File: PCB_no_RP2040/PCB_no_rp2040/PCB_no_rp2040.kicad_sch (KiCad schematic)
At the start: 7 parts, among them U1 74HC595, U2 74HC595, U3 74HC595, U4 74HC595, U5 74HC595, U6 74HC595, U7 74HC595

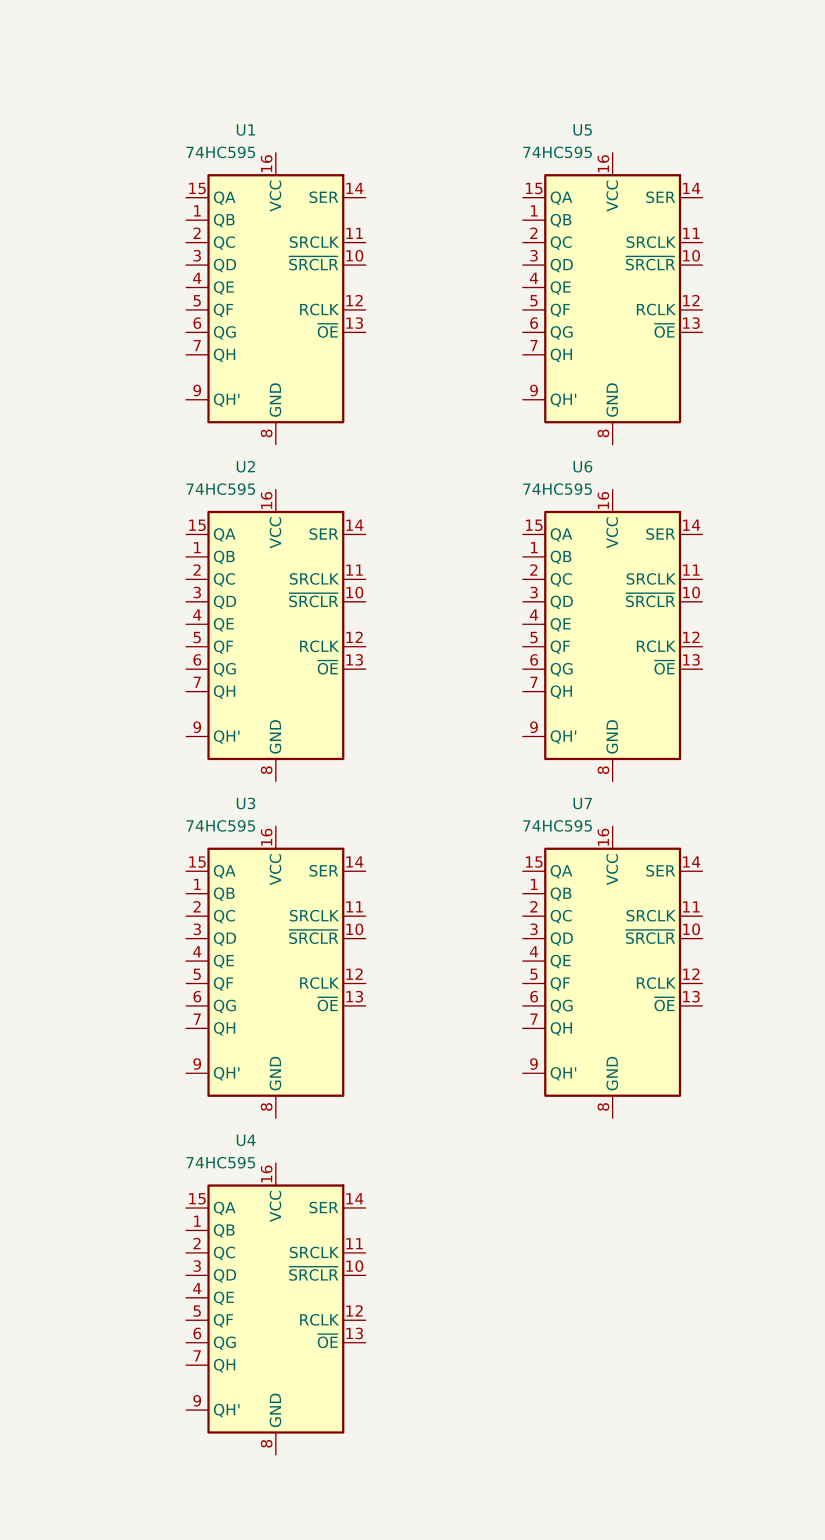
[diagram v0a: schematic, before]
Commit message: Added 4/7 shift registers and connected them to connection block, I believe this could be improved with bus lines
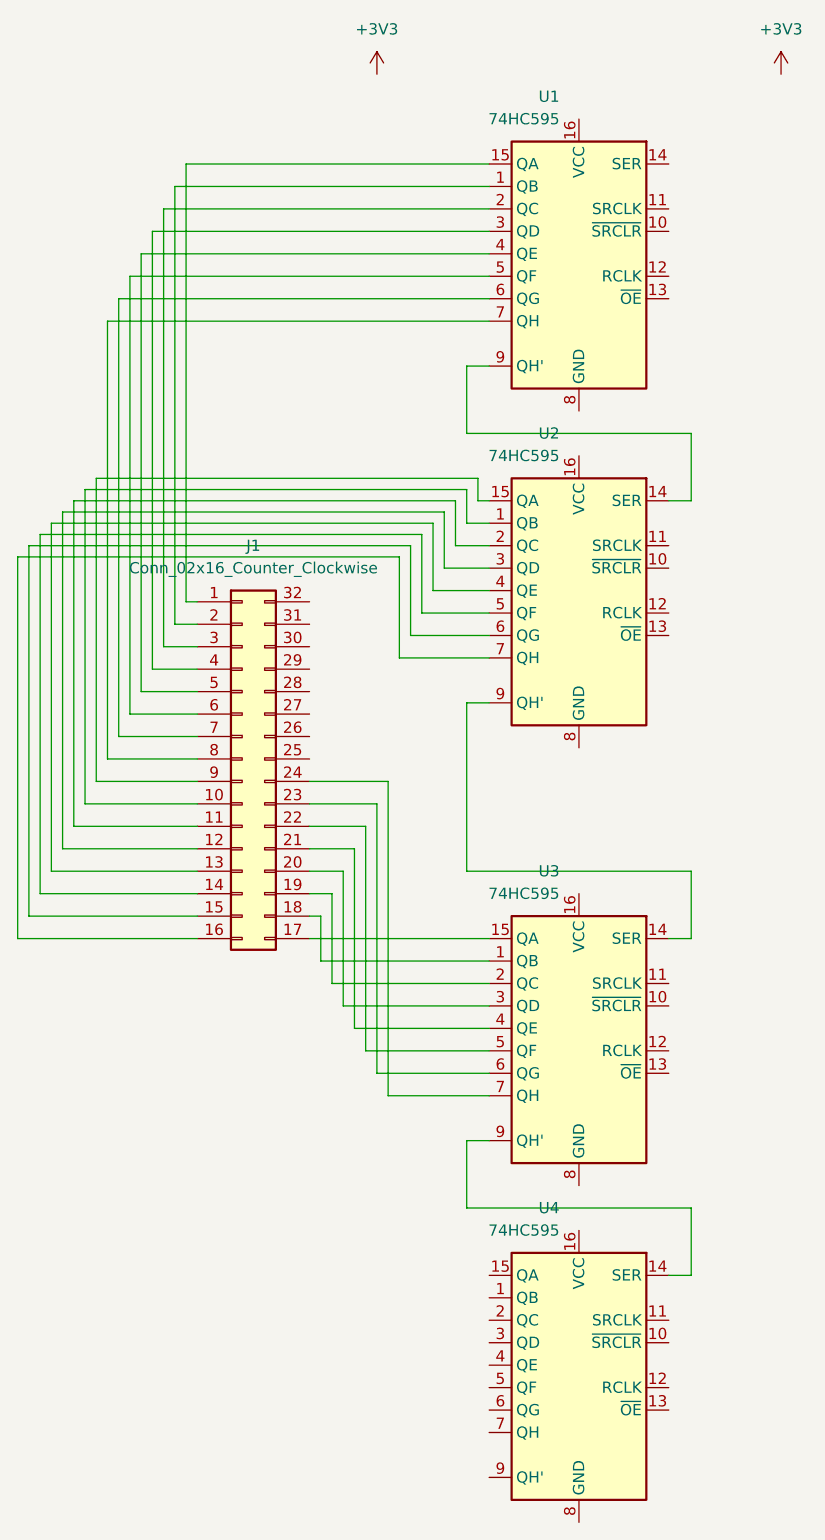
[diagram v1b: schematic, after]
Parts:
- removed U5, U6, U7: 74HC595, symbol 74xx:74HC595
- added J1: Conn_02x16_Counter_Clockwise, symbol Connector_Generic:Conn_02x16_Counter_Clockwise
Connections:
- net at U3.1 (QB): now also J1.18 (Pin_18)
- net at U3.14 (SER): now also U2.9 (QH')
- net at U3.15 (QA): now also J1.17 (Pin_17)
- net at U3.2 (QC): now also J1.19 (Pin_19)
- net at U3.3 (QD): now also J1.20 (Pin_20)
- net at U3.4 (QE): now also J1.21 (Pin_21)
- net at U3.5 (QF): now also J1.22 (Pin_22)
- net at U3.6 (QG): now also J1.23 (Pin_23)
- net at U3.7 (QH): now also J1.24 (Pin_24)
- net at U3.9 (QH'): now also U4.14 (SER)
- net at U2.1 (QB): now also J1.10 (Pin_10)
- net at U2.14 (SER): now also U1.9 (QH')
- net at U2.15 (QA): now also J1.9 (Pin_9)
- net at U2.2 (QC): now also J1.11 (Pin_11)
- net at U2.3 (QD): now also J1.12 (Pin_12)
- net at U2.4 (QE): now also J1.13 (Pin_13)
- net at U2.5 (QF): now also J1.14 (Pin_14)
- net at U2.6 (QG): now also J1.15 (Pin_15)
- net at U2.7 (QH): now also J1.16 (Pin_16)
- net at U1.1 (QB): now also J1.2 (Pin_2)
- net at U1.15 (QA): now also J1.1 (Pin_1)
- net at U1.2 (QC): now also J1.3 (Pin_3)
- net at U1.3 (QD): now also J1.4 (Pin_4)
- net at U1.4 (QE): now also J1.5 (Pin_5)
- net at U1.5 (QF): now also J1.6 (Pin_6)
- net at U1.6 (QG): now also J1.7 (Pin_7)
- net at U1.7 (QH): now also J1.8 (Pin_8)
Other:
- moved on the sheet: U1, U2, U3, U4

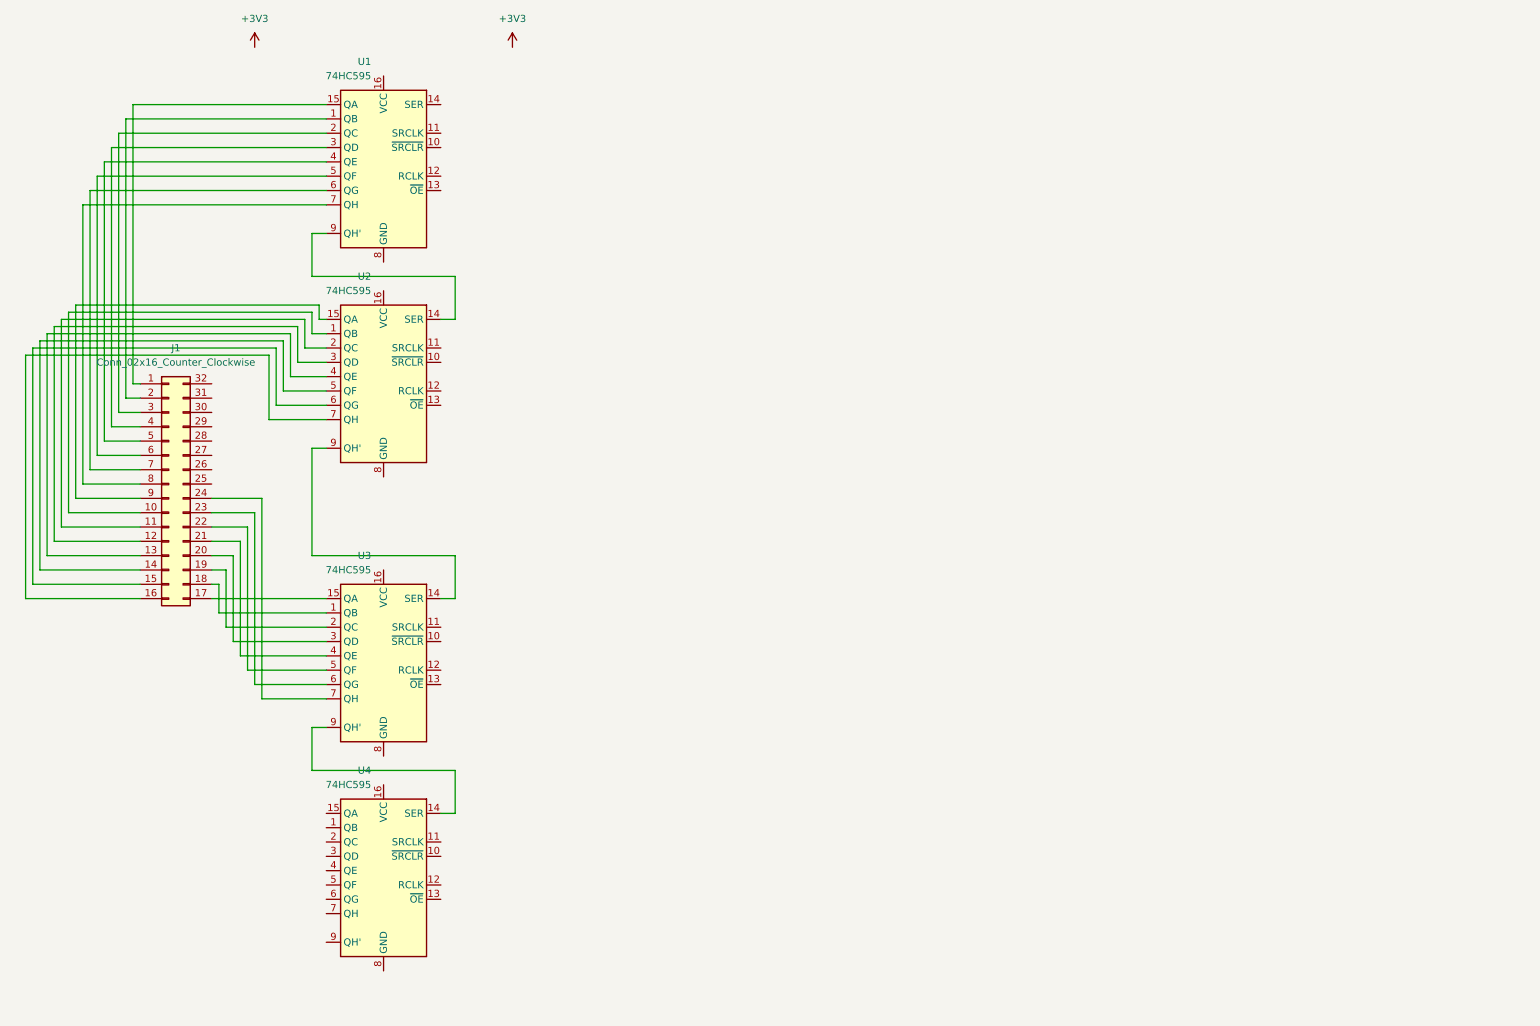
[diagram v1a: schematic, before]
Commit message: Added 7/7 shift registers with fully connected inputs and outputs, need to look into necesity of decoupling capacitor on GND
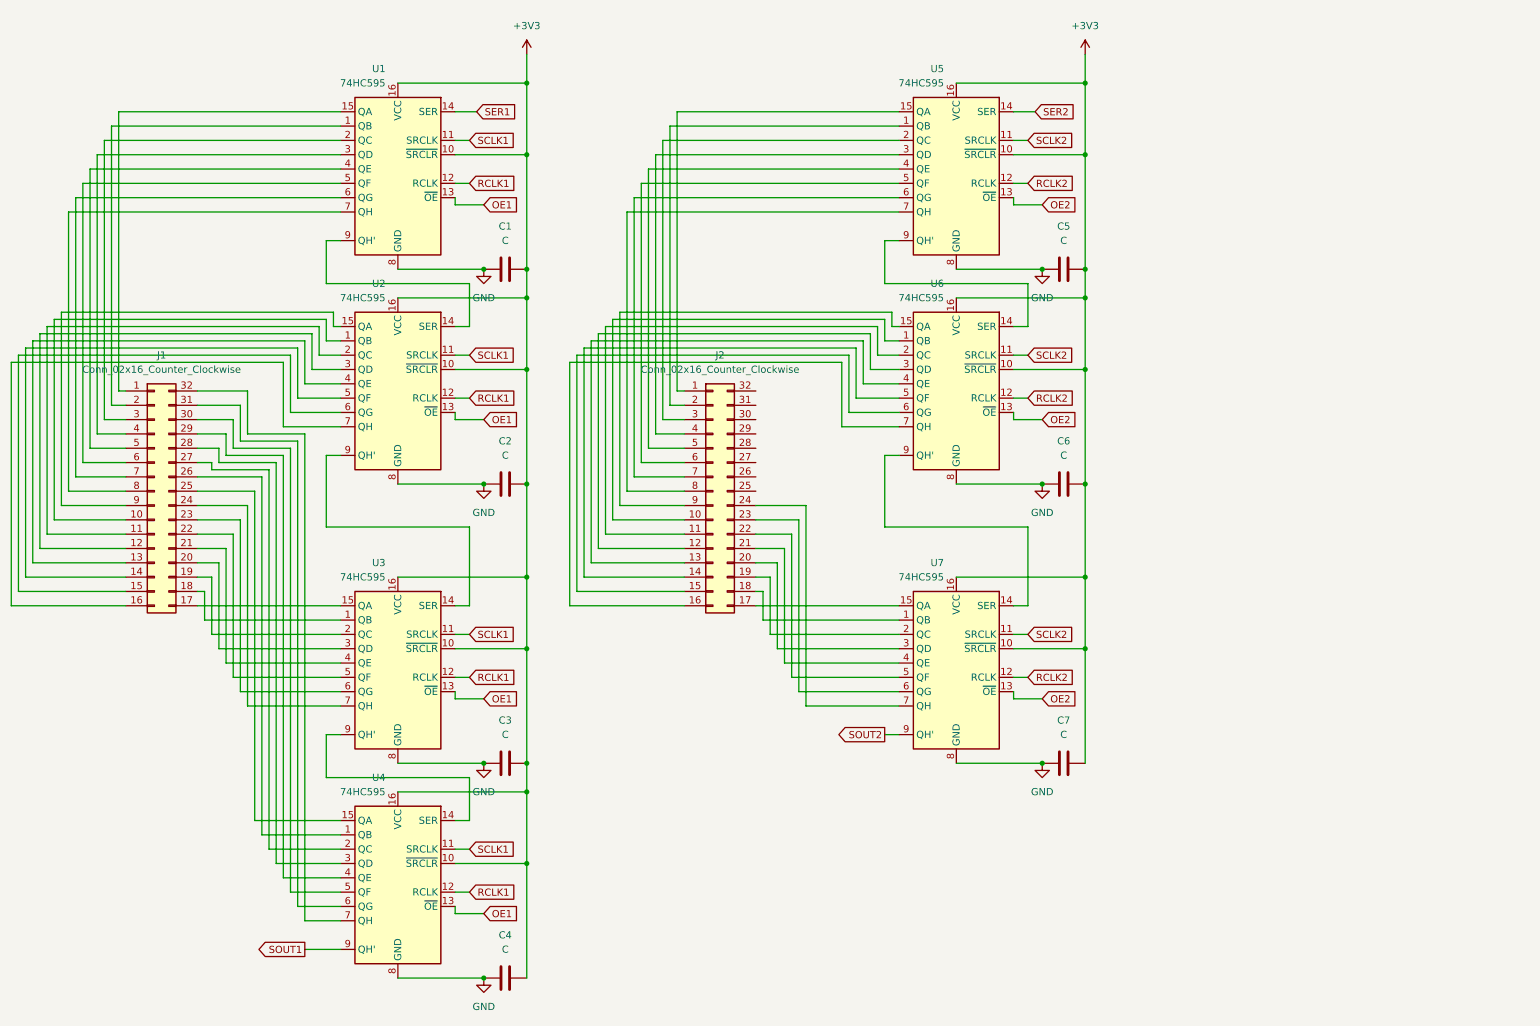
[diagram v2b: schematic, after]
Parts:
- added C1, C2, C3, C4, C5, C6, C7: C, symbol Device:C
- added J2: Conn_02x16_Counter_Clockwise, symbol Connector_Generic:Conn_02x16_Counter_Clockwise
- added U5, U6, U7: 74HC595, symbol 74xx:74HC595
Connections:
- net +3V3: now also U1.10 (~{SRCLR}), U1.16 (VCC), U2.10 (~{SRCLR}), U2.16 (VCC), U3.10 (~{SRCLR}), U3.16 (VCC), U4.10 (~{SRCLR}), U4.16 (VCC), C1.1, C2.1, C3.1, C4.1, C5.1, C6.1, C7.1, U5.10 (~{SRCLR}), U5.16 (VCC), U6.10 (~{SRCLR}), U6.16 (VCC), U7.10 (~{SRCLR}), U7.16 (VCC)
- net at J1.25 (Pin_25): now also U4.15 (QA)
- net at J1.26 (Pin_26): now also U4.1 (QB)
- net at J1.27 (Pin_27): now also U4.2 (QC)
- net at J1.28 (Pin_28): now also U4.3 (QD)
- net at J1.29 (Pin_29): now also U4.4 (QE)
- net at J1.30 (Pin_30): now also U4.5 (QF)
- net at J1.31 (Pin_31): now also U4.6 (QG)
- net at J1.32 (Pin_32): now also U4.7 (QH)
- net SCLK1: now reaches U3.11 (SRCLK)
- net SCLK1: now also U1.11 (SRCLK), U2.11 (SRCLK), U4.11 (SRCLK)
- net RCLK1: now reaches U3.12 (RCLK)
- net RCLK1: now also U1.12 (RCLK), U2.12 (RCLK), U4.12 (RCLK)
- net OE1: now reaches U3.13 (~{OE})
- net OE1: now also U1.13 (~{OE}), U2.13 (~{OE}), U4.13 (~{OE})
- net GND: now reaches U3.8 (GND)
- net GND: now also U1.8 (GND), U2.8 (GND), U4.8 (GND), C1.2, C2.2, C3.2, C4.2, C5.2, C6.2, C7.2, U5.8 (GND), U6.8 (GND), U7.8 (GND)
- net SOUT1: now reaches U4.9 (QH')
- net SER1: now reaches U1.14 (SER)
- new net: J2.2 (Pin_2), U5.1 (QB)
- new net: J2.1 (Pin_1), U5.15 (QA)
- new net: J2.3 (Pin_3), U5.2 (QC)
- new net: J2.4 (Pin_4), U5.3 (QD)
- new net: J2.5 (Pin_5), U5.4 (QE)
- new net: J2.6 (Pin_6), U5.5 (QF)
- new net: J2.7 (Pin_7), U5.6 (QG)
- new net: J2.8 (Pin_8), U5.7 (QH)
- new net: U5.9 (QH'), U6.14 (SER)
- new net: J2.18 (Pin_18), U7.1 (QB)
- new net: U6.9 (QH'), U7.14 (SER)
- new net: J2.17 (Pin_17), U7.15 (QA)
- new net: J2.19 (Pin_19), U7.2 (QC)
- new net: J2.20 (Pin_20), U7.3 (QD)
- new net: J2.21 (Pin_21), U7.4 (QE)
- new net: J2.22 (Pin_22), U7.5 (QF)
- new net: J2.23 (Pin_23), U7.6 (QG)
- new net: J2.24 (Pin_24), U7.7 (QH)
- new net: J2.10 (Pin_10), U6.1 (QB)
- new net: J2.11 (Pin_11), U6.2 (QC)
- new net: J2.12 (Pin_12), U6.3 (QD)
- new net: J2.13 (Pin_13), U6.4 (QE)
- new net: J2.14 (Pin_14), U6.5 (QF)
- new net: J2.15 (Pin_15), U6.6 (QG)
- new net: J2.16 (Pin_16), U6.7 (QH)
- new net: J2.9 (Pin_9), U6.15 (QA)
- new net OE2: U5.13 (~{OE}), U6.13 (~{OE}), U7.13 (~{OE})
- new net RCLK2: U5.12 (RCLK), U6.12 (RCLK), U7.12 (RCLK)
- new net SCLK2: U5.11 (SRCLK), U6.11 (SRCLK), U7.11 (SRCLK)
- new net SER2: U5.14 (SER)
- new net SOUT2: U7.9 (QH')
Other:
- moved on the sheet: J1, U1, U2, U3, U4

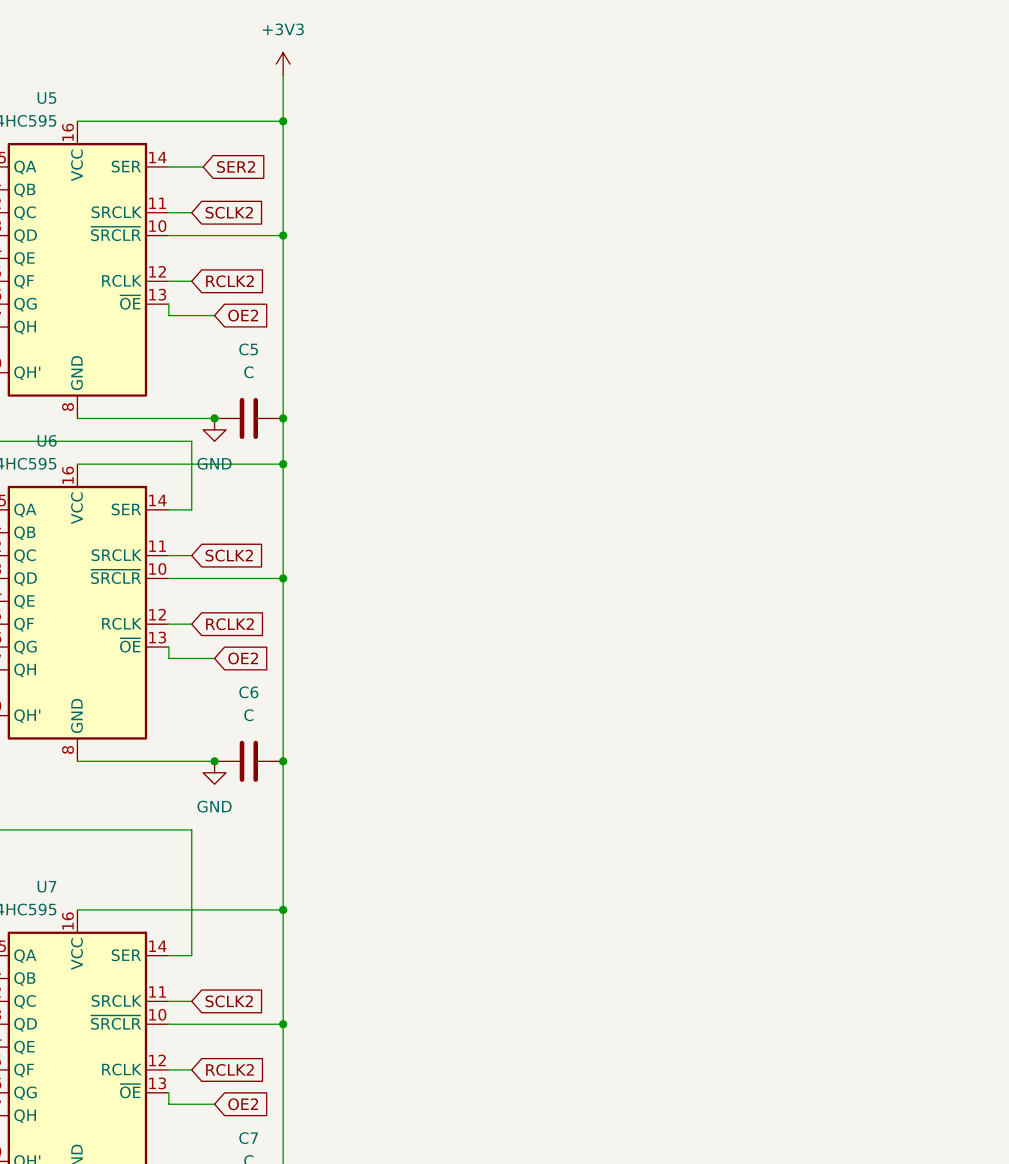
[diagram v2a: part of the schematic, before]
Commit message: Added both ADC's connected all inputs that connect to the mat, but need to look into what other pins do before connecting them
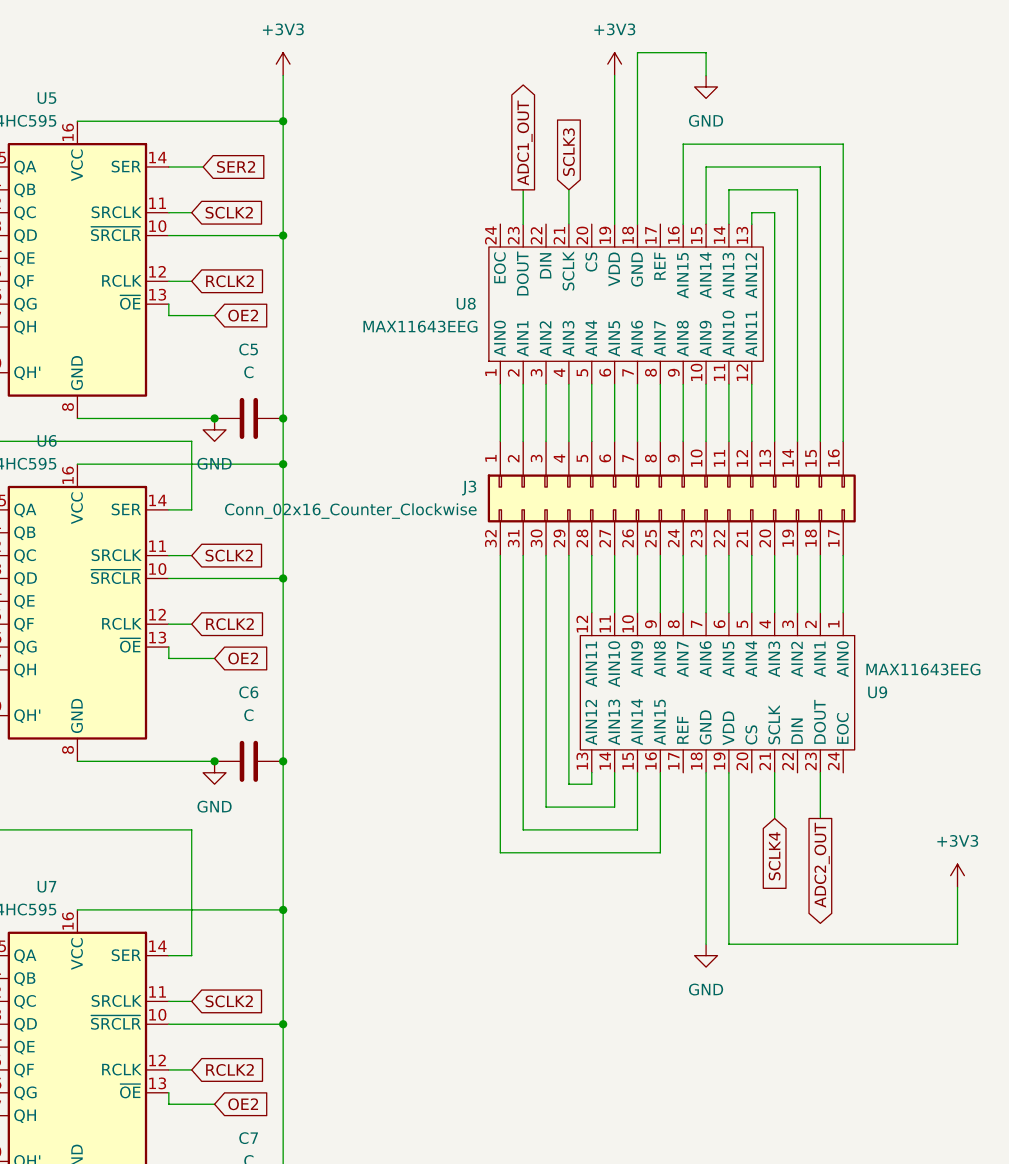
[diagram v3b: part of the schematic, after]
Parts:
- added J3: Conn_02x16_Counter_Clockwise, symbol Connector_Generic:Conn_02x16_Counter_Clockwise
- added U8, U9: MAX11643EEG, symbol Capstone_Library:MAX11643EEG
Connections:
- net +3V3: now also U8.19 (VDD), U9.19 (VDD)
- net GND: now also U8.18 (GND), U9.18 (GND)
- new net: J3.1 (Pin_1), U8.1 (AIN0)
- new net: J3.10 (Pin_10), U8.10 (AIN9)
- new net: J3.11 (Pin_11), U8.11 (AIN10)
- new net: J3.12 (Pin_12), U8.12 (AIN11)
- new net: J3.13 (Pin_13), U8.13 (AIN12)
- new net: J3.14 (Pin_14), U8.14 (AIN13)
- new net: J3.15 (Pin_15), U8.15 (AIN14)
- new net: J3.16 (Pin_16), U8.16 (AIN15)
- new net: J3.17 (Pin_17), U9.1 (AIN0)
- new net: J3.18 (Pin_18), U9.2 (AIN1)
- new net: J3.19 (Pin_19), U9.3 (AIN2)
- new net: J3.2 (Pin_2), U8.2 (AIN1)
- new net: J3.20 (Pin_20), U9.4 (AIN3)
- new net: J3.21 (Pin_21), U9.5 (AIN4)
- new net: J3.22 (Pin_22), U9.6 (AIN5)
- new net: J3.23 (Pin_23), U9.7 (AIN6)
- new net: J3.24 (Pin_24), U9.8 (AIN7)
- new net: J3.25 (Pin_25), U9.9 (AIN8)
- new net: J3.26 (Pin_26), U9.10 (AIN9)
- new net: J3.27 (Pin_27), U9.11 (AIN10)
- new net: J3.28 (Pin_28), U9.12 (AIN11)
- new net: J3.29 (Pin_29), U9.13 (AIN12)
- new net: J3.3 (Pin_3), U8.3 (AIN2)
- new net: J3.30 (Pin_30), U9.14 (AIN13)
- new net: J3.31 (Pin_31), U9.15 (AIN14)
- new net: J3.32 (Pin_32), U9.16 (AIN15)
- new net: J3.4 (Pin_4), U8.4 (AIN3)
- new net: J3.5 (Pin_5), U8.5 (AIN4)
- new net: J3.6 (Pin_6), U8.6 (AIN5)
- new net: J3.7 (Pin_7), U8.7 (AIN6)
- new net: J3.8 (Pin_8), U8.8 (AIN7)
- new net: J3.9 (Pin_9), U8.9 (AIN8)
- new net ADC1_OUT: U8.23 (DOUT)
- new net ADC2_OUT: U9.23 (DOUT)
- new net SCLK3: U8.21 (SCLK)
- new net SCLK4: U9.21 (SCLK)
